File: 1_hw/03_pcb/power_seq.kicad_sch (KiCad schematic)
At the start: 1 part

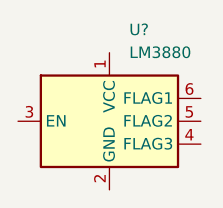
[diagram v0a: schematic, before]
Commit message: FEAT: Finished Excel Pin Map for MCU. Completed MCU + FPGA in Schematic.
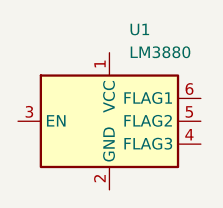
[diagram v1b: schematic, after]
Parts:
- gave numbers to parts that had none: 1
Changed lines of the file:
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@@
 		(dnp no)
 		(fields_autoplaced yes)
-		(property "Reference" "U?"
+		(property "Reference" "U1"
 			(at 94.9041 82.55 0)
 			(effects
@@
 			(project ""
 				(path "/866ef9be-3b01-4288-a6e0-a2357aa17e50/3081f01b-0fc6-40b1-9db3-1dae5b3adecb"
-					(reference "U?")
+					(reference "U1")
 					(unit 1)
 				)

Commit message: FEAT: Added USB ESD Protection.
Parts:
- removed U1: LM3880, Package_TO_SOT_SMD:SOT-23-6, symbol Power_Supervisor:LM3880
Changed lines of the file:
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@@
 		(company "Tomasz Brzyzek")
 	)
-	(symbol
-		(lib_id "Power_Supervisor:LM3880")
-		(at 92.71 92.71 0)
-		(unit 1)
-		(exclude_from_sim no)
-		(in_bom yes)
-		(on_board yes)
-		(dnp no)
-		(fields_autoplaced yes)
-		(property "Reference" "U1"
-			(at 94.9041 82.55 0)
-			(effects
-				(font
-					(size 1.27 1.27)
-				)
-				(justify left)
-			)
-		)
-		(property "Value" "LM3880"
-			(at 94.9041 85.09 0)
-			(effects
-				(font
-					(size 1.27 1.27)
-				)
-				(justify left)
-			)
-		)
-		(property "Footprint" "Package_TO_SOT_SMD:SOT-23-6"
-			(at 109.22 99.06 0)
-			(effects
-				(font
-					(size 1.27 1.27)
-				)
-				(hide yes)
-			)
-		)
-		(property "Datasheet" "http://www.ti.com/lit/ds/symlink/lm3880.pdf"
-			(at 92.71 92.71 0)
-			(effects
-				(font
-					(size 1.27 1.27)
-				)
-				(hide yes)
-			)
-		)
-		(property "Description" "Simple Power Sequencer, SOT-23-6"
-			(at 92.71 92.71 0)
-			(effects
-				(font
-					(size 1.27 1.27)
-				)
-				(hide yes)
-			)
-		)
-		(pin "2"
-		)
-		(pin "1"
-		)
-		(pin "4"
-		)
-		(pin "3"
-		)
-		(pin "6"
-		)
-		(pin "5"
-		)
-		(instances
-			(project ""
-				(path "/866ef9be-3b01-4288-a6e0-a2357aa17e50/3081f01b-0fc6-40b1-9db3-1dae5b3adecb"
-					(reference "U1")
-					(unit 1)
-				)
-			)
-		)
-	)
 )
